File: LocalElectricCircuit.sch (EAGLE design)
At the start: 42 parts, among them IC1 PIC32MX360F512L, J1 Prog. Port, U1 ADS1118, U2 ADS1118, X2 MALE_VGA

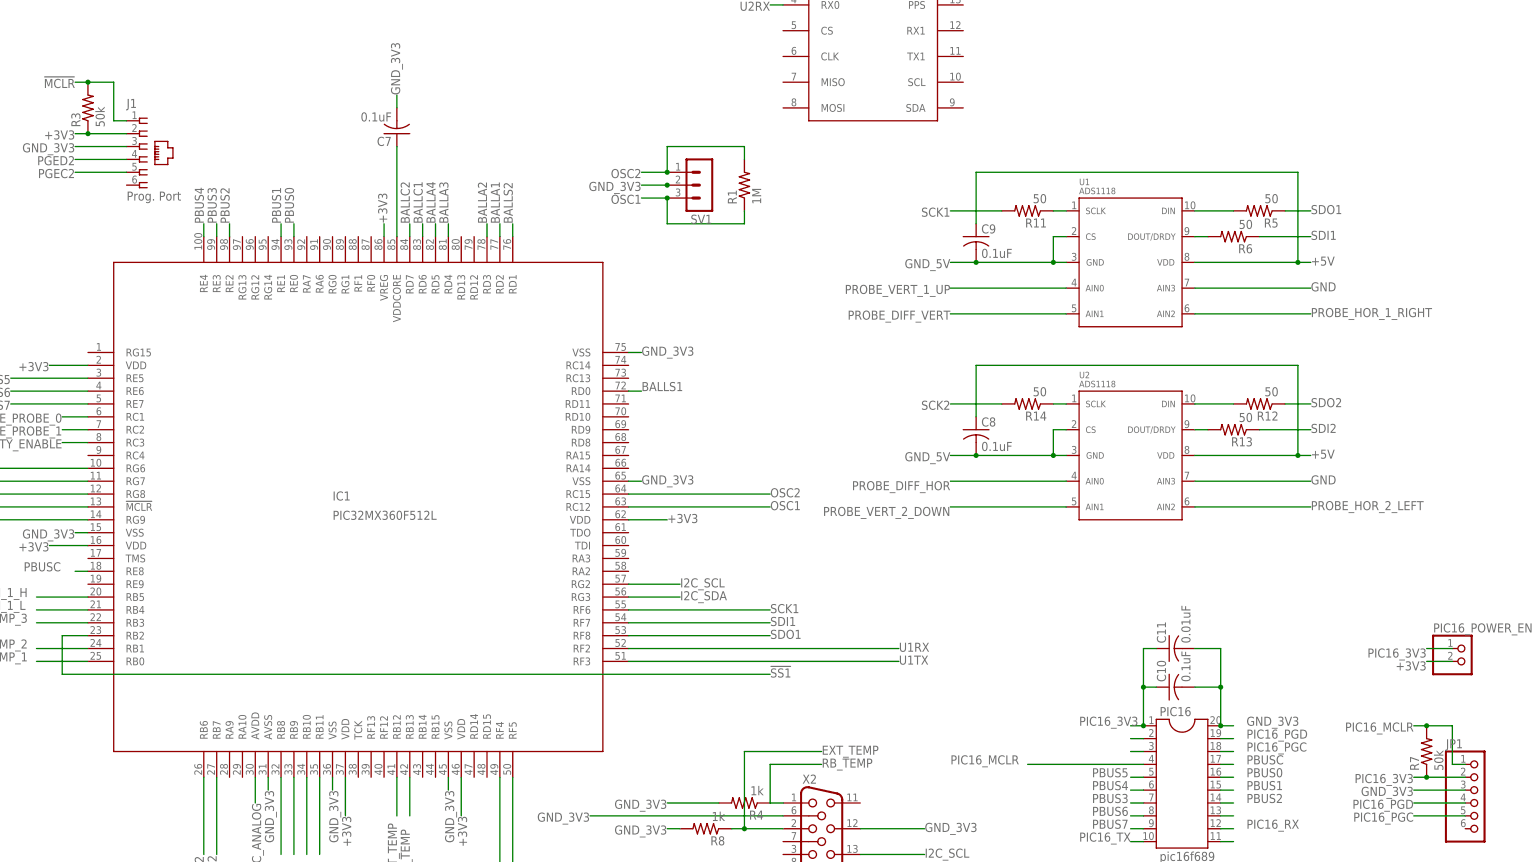
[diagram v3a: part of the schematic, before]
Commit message: Update silk screen with REv 1.0 and date Added fan out for all PIC pins Began on fan out for ADC pins ETC.
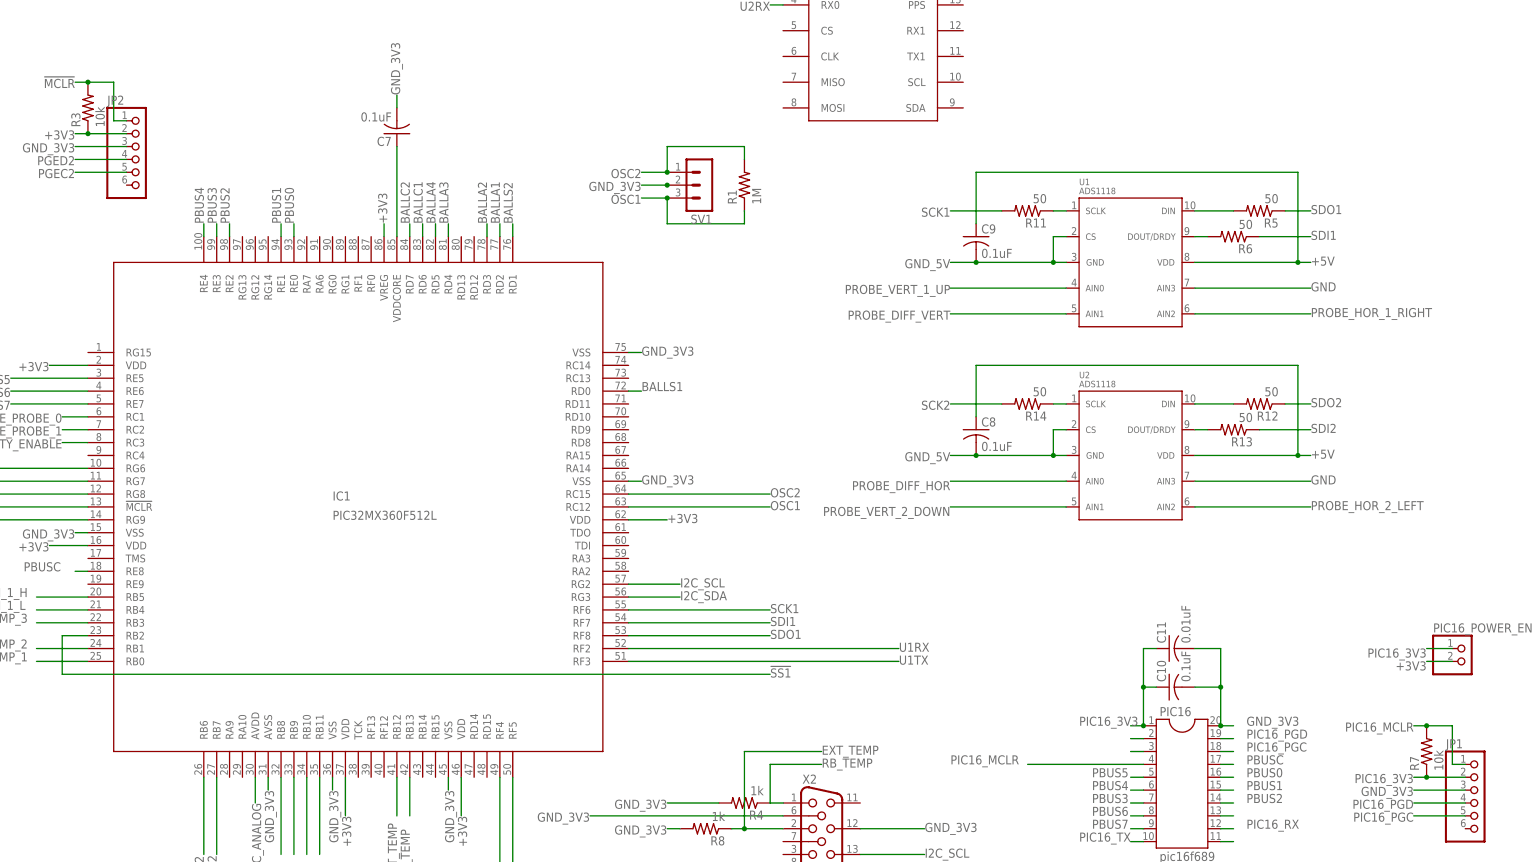
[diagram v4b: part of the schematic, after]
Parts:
- removed J1: Prog. Port, con-amp:520258-3
- added JP2: (no value), pinhead:PINHD-1X6
- R3, R7: value 50k -> 10k
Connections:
- net !MCLR: now also JP2.1; no longer J1.1
- net +3V3: now also JP2.2; no longer J1.2
- net GND_3V3: now also JP2.3; no longer J1.3
- net PGEC2: now also JP2.5; no longer J1.5
- net PGED2: now also JP2.4; no longer J1.4
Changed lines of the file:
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@@
 <part name="U$1" library="SparkfunVenusGPSBreakout" deviceset="SPARKFUN_VENUS_GPS_BREAKOUT" device=""/>
 <part name="C7" library="resistor" deviceset="C-US" device="C1206" value="0.1uF"/>
-<part name="J1" library="con-amp" deviceset="520258-3" device="" value="Prog. Port"/>
-<part name="R3" library="rcl" deviceset="R-US_" device="M1206" value="50k"/>
+<part name="R3" library="rcl" deviceset="R-US_" device="M1206" value="10k"/>
 <part name="J2" library="19inch_VG96KB" deviceset="VG96" device="KB"/>
 <part name="X1" library="con-subd" deviceset="HF15" device="H"/>
@@
 <part name="C10" library="resistor" deviceset="C-US" device="C1206" value="0.1uF"/>
 <part name="C11" library="resistor" deviceset="C-US" device="C1206" value="0.01uF"/>
-<part name="R7" library="rcl" deviceset="R-US_" device="M1206" value="50k"/>
+<part name="R7" library="rcl" deviceset="R-US_" device="M1206" value="10k"/>
 <part name="C12" library="resistor" deviceset="C-US" device="C1206" value="0.01uF"/>
 <part name="C13" library="resistor" deviceset="C-US" device="C1206" value="0.01uF"/>
@@
 <part name="JP1" library="pinhead" deviceset="PINHD-1X6" device=""/>
 <part name="X2" library="MALE_VGA" deviceset="MALE_VGA" device=""/>
+<part name="JP2" library="pinhead" deviceset="PINHD-1X6" device=""/>
 </parts>
 <sheets>
@@
 <instance part="U$1" gate="G$1" x="172.72" y="157.48"/>
 <instance part="C7" gate="G$1" x="78.74" y="134.62" rot="R180"/>
-<instance part="J1" gate="G$1" x="27.94" y="132.08"/>
 <instance part="R3" gate="G$1" x="17.78" y="139.7" rot="R90"/>
 <instance part="J2" gate="G$1" x="-35.56" y="66.04" rot="MR0"/>
@@
 <instance part="JP1" gate="A" x="292.1" y="2.54"/>
 <instance part="X2" gate="G$1" x="162.56" y="-7.62"/>
+<instance part="JP2" gate="A" x="27.94" y="129.54"/>
 </instances>
 <busses>
@@
 </segment>
 <segment>
-<pinref part="J1" gate="G$1" pin="2"/>
 <wire x1="25.4" y1="134.62" x2="17.78" y2="134.62" width="0.1524" layer="91"/>
 <pinref part="R3" gate="G$1" pin="1"/>
@@
 <junction x="17.78" y="134.62"/>
 <label x="15.24" y="135.255" size="1.778" layer="95" rot="R180"/>
+<pinref part="JP2" gate="A" pin="2"/>
 </segment>
 <segment>
@@
 </segment>
 <segment>
-<pinref part="J1" gate="G$1" pin="3"/>
 <wire x1="25.4" y1="132.08" x2="15.24" y2="132.08" width="0.1524" layer="91"/>
 <label x="15.24" y="132.715" size="1.778" layer="95" rot="R180"/>
+<pinref part="JP2" gate="A" pin="3"/>
 </segment>
 <segment>
@@
 <net name="!MCLR" class="0">
 <segment>
-<pinref part="J1" gate="G$1" pin="1"/>
-<wire x1="25.4" y1="137.16" x2="22.86" y2="137.16" width="0.1524" layer="91"/>
 <wire x1="22.86" y1="137.16" x2="22.86" y2="144.78" width="0.1524" layer="91"/>
 <wire x1="22.86" y1="144.78" x2="17.78" y2="144.78" width="0.1524" layer="91"/>
@@
 <junction x="17.78" y="144.78"/>
 <label x="15.24" y="145.415" size="1.778" layer="95" rot="R180"/>
+<pinref part="JP2" gate="A" pin="1"/>
+<wire x1="25.4" y1="137.16" x2="22.86" y2="137.16" width="0.1524" layer="91"/>
 </segment>
 <segment>
@@
 <net name="PGEC2" class="0">
 <segment>
-<pinref part="J1" gate="G$1" pin="5"/>
 <wire x1="25.4" y1="127" x2="15.24" y2="127" width="0.1524" layer="91"/>
 <label x="15.24" y="127.635" size="1.778" layer="95" rot="R180"/>
+<pinref part="JP2" gate="A" pin="5"/>
 </segment>
 <segment>
@@
 <net name="PGED2" class="0">
 <segment>
-<pinref part="J1" gate="G$1" pin="4"/>
 <wire x1="25.4" y1="129.54" x2="15.24" y2="129.54" width="0.1524" layer="91"/>
 <label x="15.24" y="130.175" size="1.778" layer="95" rot="R180"/>
-</segment>
-<segment>
+<pinref part="JP2" gate="A" pin="4"/>
+</segment>
+<segment>

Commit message: Did a whole ton of stuff. Added the level-shifting hardware Added fan out for ADC's Worked on clearing some DRC errors ETC
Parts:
- added JP3, JP4, JP5, JP6: (no value), pinhead:PINHD-1X5
- added R10, R17: 680, resistor:R-US_R1206
- added R16, R9: 510, resistor:R-US_R1206
- added V1, V2: 74125N, 74ttl-din:74125N
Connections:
- new net ADC1_DIN: JP3.5, R5.1, V1/2.Y
- new net ADC1_DIVIDED: R10.2, R9.1, V1/3.A
- new net ADC1_DOUT: JP3.4, R6.1, R9.2
- new net ADC1_SCK: JP4.1, R11.2, V1/1.Y
- new net ADC2_DIN: JP5.5, R12.1, V2/2.Y
- new net ADC2_DIVIDED: R16.1, R17.2, V2/3.A
- new net ADC2_DOUT: JP5.4, R13.1, R16.2
- new net ADC2_SCK: JP6.1, R14.2, V2/1.Y
- net +5V: now also JP3.3, JP5.3, V1/+UB.+UB, V2/+UB.+UB
- net GND: now also JP3.2, JP5.2
- net GND_5V: now also JP4.2, JP4.3, JP6.2, JP6.3, R10.1, R17.1, V1/-UB.-UB, V1/1.!G, V1/2.!G, V1/3.!G, V1/4.!G, V1/4.A, V1/4.Y, V2/-UB.-UB, V2/1.!G, V2/2.!G, V2/3.!G, V2/4.!G, V2/4.A, V2/4.Y
- net PROBE_DIFF_HOR: now also JP6.4
- net PROBE_DIFF_VERT: now also JP4.5
- net PROBE_HOR_1_RIGHT: now also JP3.1
- net PROBE_HOR_2_LEFT: now also JP5.1
- net PROBE_VERT_1_UP: now also JP4.4
- net PROBE_VERT_2_DOWN: now also JP6.5
- net SCK1: now also V1/1.A; no longer R11.2
- net SCK2: now also V2/1.A; no longer R14.2
- net SDI1: now also V1/3.Y; no longer R6.1
- net SDI2: now also V2/3.Y; no longer R13.1
- net SDO1: now also V1/2.A; no longer R5.1
- net SDO2: now also V2/2.A; no longer R12.1
- net U2RX: now also U$1.TX0; no longer U$1.RX0
- net U2TX: now also U$1.RX0; no longer U$1.TX0
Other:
- moved on the sheet: C8, C9, R11, R12, R13, R14, R5, R6, U1, U2

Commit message: Pre auto-route
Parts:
- removed R15, R4, R8: 1k, rcl:R-US_0309/12
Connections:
- new net PIC_COND_EN: IC1.RC3, V2/4.A
- net +3V3: no longer R15.1
- net CONDUCTIVITY_ENABLE: now also V2/4.Y; no longer IC1.RC3, R15.2
- net EXT_TEMP: no longer R8.1
- net GND_3V3: no longer R4.2, R8.2
- net GND_5V: no longer V1/4.A, V2/4.A, V2/4.Y
- net RB_TEMP: no longer R4.1
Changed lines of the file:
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@@
 <part name="C16" library="resistor" deviceset="C-US" device="C1206" value="0.01uF"/>
 <part name="C17" library="resistor" deviceset="C-US" device="C1206" value="0.01uF"/>
-<part name="R4" library="rcl" deviceset="R-US_" device="0309/12" value="1k"/>
-<part name="R8" library="rcl" deviceset="R-US_" device="0309/12" value="1k"/>
 <part name="R5" library="rcl" deviceset="R-US_" device="M1206" value="50"/>
 <part name="R6" library="rcl" deviceset="R-US_" device="M1206" value="50"/>
@@
 <part name="R14" library="rcl" deviceset="R-US_" device="M1206" value="50"/>
 <part name="PIC16_POWER_EN" library="pinhead" deviceset="PINHD-1X2" device=""/>
-<part name="R15" library="rcl" deviceset="R-US_" device="0309/12" value="1k"/>
 <part name="JP1" library="pinhead" deviceset="PINHD-1X6" device=""/>
 <part name="X2" library="MALE_VGA" deviceset="MALE_VGA" device=""/>
@@
 <instance part="C16" gate="G$1" x="91.44" y="210.82"/>
 <instance part="C17" gate="G$1" x="121.92" y="210.82"/>
-<instance part="R4" gate="G$1" x="147.32" y="2.54" rot="R180"/>
-<instance part="R8" gate="G$1" x="139.7" y="-2.54" rot="R180"/>
 <instance part="R5" gate="G$1" x="337.82" y="213.36" rot="R180"/>
 <instance part="R6" gate="G$1" x="332.74" y="208.28" rot="R180"/>
@@
 <instance part="R14" gate="G$1" x="292.1" y="114.3" rot="R180"/>
 <instance part="PIC16_POWER_EN" gate="G$1" x="289.56" y="30.48"/>
-<instance part="R15" gate="G$1" x="231.14" y="-73.66" rot="R180"/>
 <instance part="JP1" gate="A" x="292.1" y="2.54"/>
 <instance part="X2" gate="G$1" x="162.56" y="-7.62"/>
@@
 <wire x1="76.2" y1="114.3" x2="76.2" y2="116.84" width="0.1524" layer="91"/>
 <label x="76.835" y="116.84" size="1.778" layer="95" rot="R90"/>
-</segment>
-<segment>
-<label x="241.935" y="-63.5" size="1.778" layer="95" rot="R90"/>
-<pinref part="R15" gate="G$1" pin="1"/>
-<wire x1="236.22" y1="-73.66" x2="241.3" y2="-73.66" width="0.1524" layer="91"/>
-<wire x1="241.3" y1="-73.66" x2="241.3" y2="-63.5" width="0.1524" layer="91"/>
 </segment>
 </net>
@@
 </segment>
 <segment>
-<pinref part="R4" gate="G$1" pin="2"/>
-<wire x1="142.24" y1="2.54" x2="132.08" y2="2.54" width="0.1524" layer="91"/>
-<label x="132.08" y="3.175" size="1.778" layer="95" rot="R180"/>
-</segment>
-<segment>
-<pinref part="R8" gate="G$1" pin="2"/>
-<wire x1="134.62" y1="-2.54" x2="132.08" y2="-2.54" width="0.1524" layer="91"/>
-<label x="132.08" y="-1.905" size="1.778" layer="95" rot="R180"/>
-</segment>
-<segment>
 <wire x1="154.94" y1="0" x2="116.84" y2="0" width="0.1524" layer="91"/>
 <label x="116.84" y="0.635" size="1.778" layer="95" rot="R180"/>
@@
 </segment>
 <segment>
-<pinref part="V2" gate="/4" pin="A"/>
-<wire x1="378.46" y1="99.06" x2="370.84" y2="99.06" width="0.1524" layer="91"/>
-<label x="370.84" y="99.695" size="1.778" layer="95" rot="R180"/>
-</segment>
-<segment>
-<pinref part="V2" gate="/4" pin="Y"/>
-<wire x1="398.78" y1="101.6" x2="406.4" y2="101.6" width="0.1524" layer="91"/>
-<label x="406.4" y="100.965" size="1.778" layer="95"/>
-</segment>
-<segment>
 <pinref part="R10" gate="G$1" pin="1"/>
 <wire x1="431.8" y1="228.6" x2="431.8" y2="231.14" width="0.1524" layer="91"/>
@@
 <wire x1="381" y1="203.2" x2="373.38" y2="203.2" width="0.1524" layer="91"/>
 <label x="373.38" y="203.835" size="1.778" layer="95" rot="R180"/>
-</segment>
-<segment>
-<pinref part="V1" gate="/4" pin="A"/>
-<wire x1="381" y1="198.12" x2="373.38" y2="198.12" width="0.1524" layer="91"/>
-<label x="373.38" y="198.755" size="1.778" layer="95" rot="R180"/>
 </segment>
 <segment>
@@
 <segment>
 <label x="162.56" y="12.065" size="1.778" layer="95"/>
-<pinref part="R8" gate="G$1" pin="1"/>
-<wire x1="147.32" y1="-2.54" x2="144.78" y2="-2.54" width="0.1524" layer="91"/>
 <wire x1="147.32" y1="-2.54" x2="147.32" y2="12.7" width="0.1524" layer="91"/>
 <wire x1="147.32" y1="12.7" x2="162.56" y2="12.7" width="0.1524" layer="91"/>
 <wire x1="154.94" y1="-2.54" x2="147.32" y2="-2.54" width="0.1524" layer="91"/>
-<junction x="147.32" y="-2.54"/>
 <pinref part="X2" gate="G$1" pin="2"/>
 </segment>
@@
 <segment>
 <label x="162.56" y="9.525" size="1.778" layer="95"/>
-<pinref part="R4" gate="G$1" pin="1"/>
 <wire x1="152.4" y1="2.54" x2="152.4" y2="10.16" width="0.1524" layer="91"/>
 <wire x1="152.4" y1="10.16" x2="162.56" y2="10.16" width="0.1524" layer="91"/>
@@
 <net name="CONDUCTIVITY_ENABLE" class="0">
 <segment>
-<label x="220.98" y="-73.025" size="1.778" layer="95" rot="R180"/>
-<pinref part="R15" gate="G$1" pin="2"/>
-<wire x1="220.98" y1="-73.66" x2="226.06" y2="-73.66" width="0.1524" layer="91"/>
-<wire x1="226.06" y1="-73.66" x2="226.06" y2="-83.82" width="0.1524" layer="91"/>
-<wire x1="226.06" y1="-83.82" x2="248.92" y2="-83.82" width="0.1524" layer="91"/>
-<junction x="226.06" y="-73.66"/>
-<label x="248.92" y="-84.455" size="1.778" layer="95"/>
-</segment>
-<segment>
-<pinref part="IC1" gate="G$1" pin="RC3"/>
-<wire x1="17.78" y1="73.66" x2="12.7" y2="73.66" width="0.1524" layer="91"/>
-<label x="12.7" y="74.295" size="1.778" layer="95" rot="R180"/>
-</segment>
-<segment>
 <pinref part="J2" gate="G$1" pin="C14"/>
 <wire x1="-45.72" y1="71.12" x2="-55.88" y2="71.12" width="0.1524" layer="91"/>
 <label x="-55.88" y="71.755" size="1.778" layer="95" rot="R180"/>
+</segment>
+<segment>
+<pinref part="V2" gate="/4" pin="Y"/>
+<wire x1="398.78" y1="101.6" x2="406.4" y2="101.6" width="0.1524" layer="91"/>
+<label x="406.4" y="100.965" size="1.778" layer="95"/>
 </segment>
 </net>
@@
 </segment>
 </net>
+<net name="PIC_COND_EN" class="0">
+<segment>
+<pinref part="IC1" gate="G$1" pin="RC3"/>
+<wire x1="17.78" y1="73.66" x2="12.7" y2="73.66" width="0.1524" layer="91"/>
+<label x="12.7" y="74.295" size="1.778" layer="95" rot="R180"/>
+</segment>
+<segment>
+<pinref part="V2" gate="/4" pin="A"/>
+<wire x1="378.46" y1="99.06" x2="370.84" y2="99.06" width="0.1524" layer="91"/>
+<label x="370.84" y="99.695" size="1.778" layer="95" rot="R180"/>
+</segment>
+</net>

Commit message: Ugh🎈
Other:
- moved on the sheet: C8, C9, JP3, JP4, JP5, JP6, R10, R11, R12, R13, R14, R16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
